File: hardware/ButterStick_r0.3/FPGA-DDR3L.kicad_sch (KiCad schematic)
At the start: 1 part, among them U2 ECP5UM5G_85_CABGA381

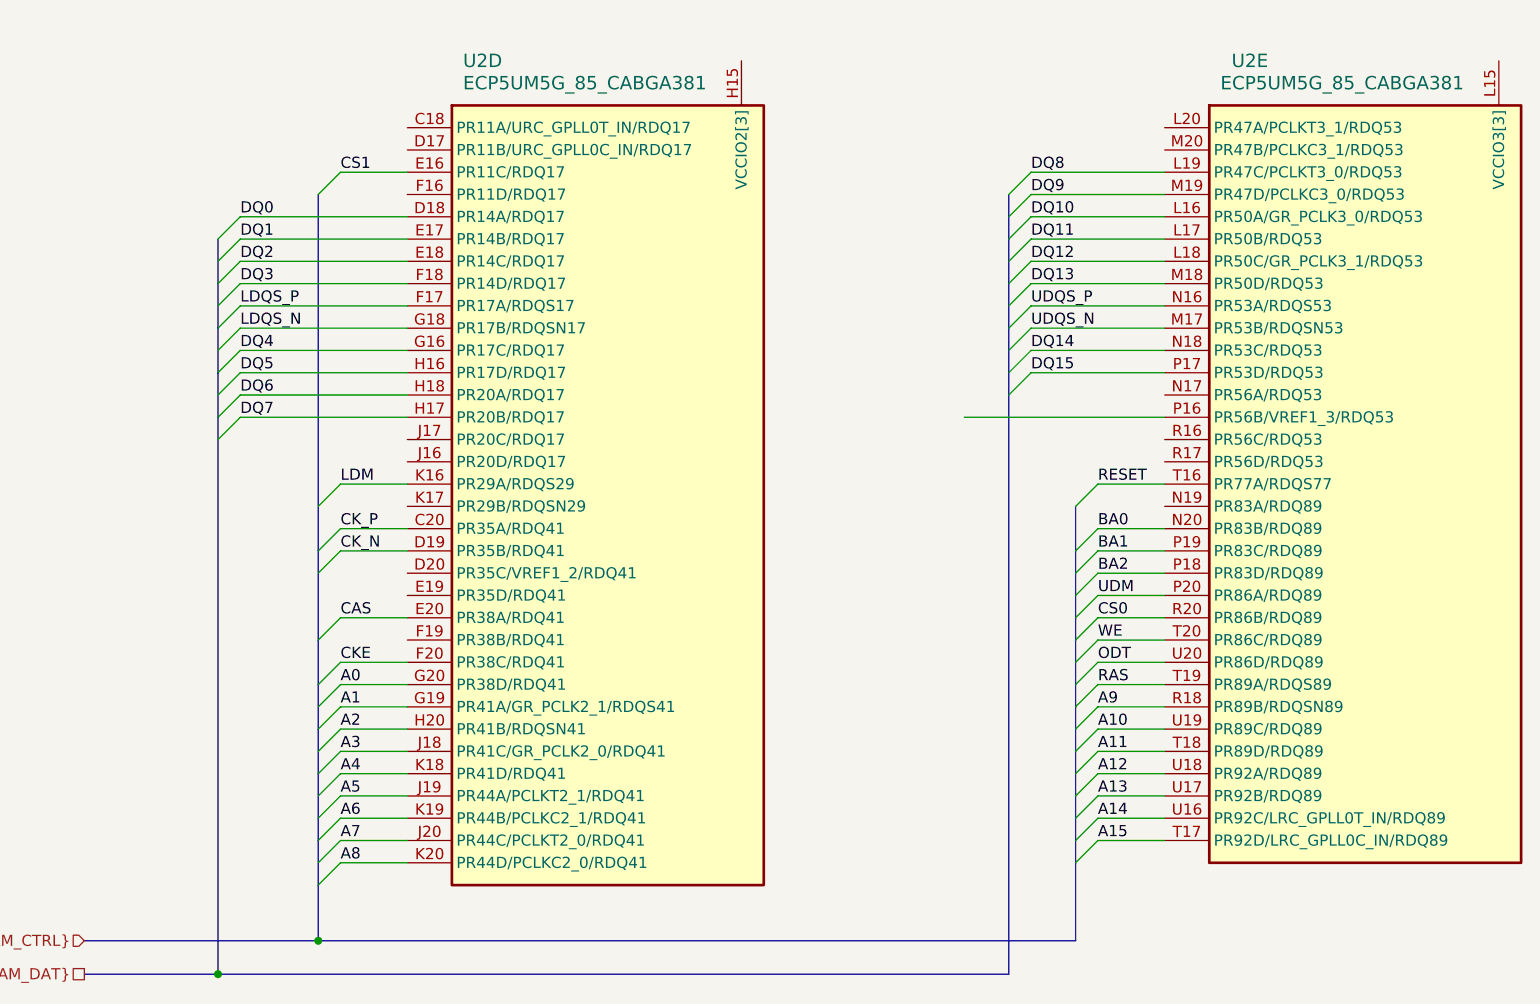
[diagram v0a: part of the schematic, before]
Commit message: hw.r0_3: routing improvements
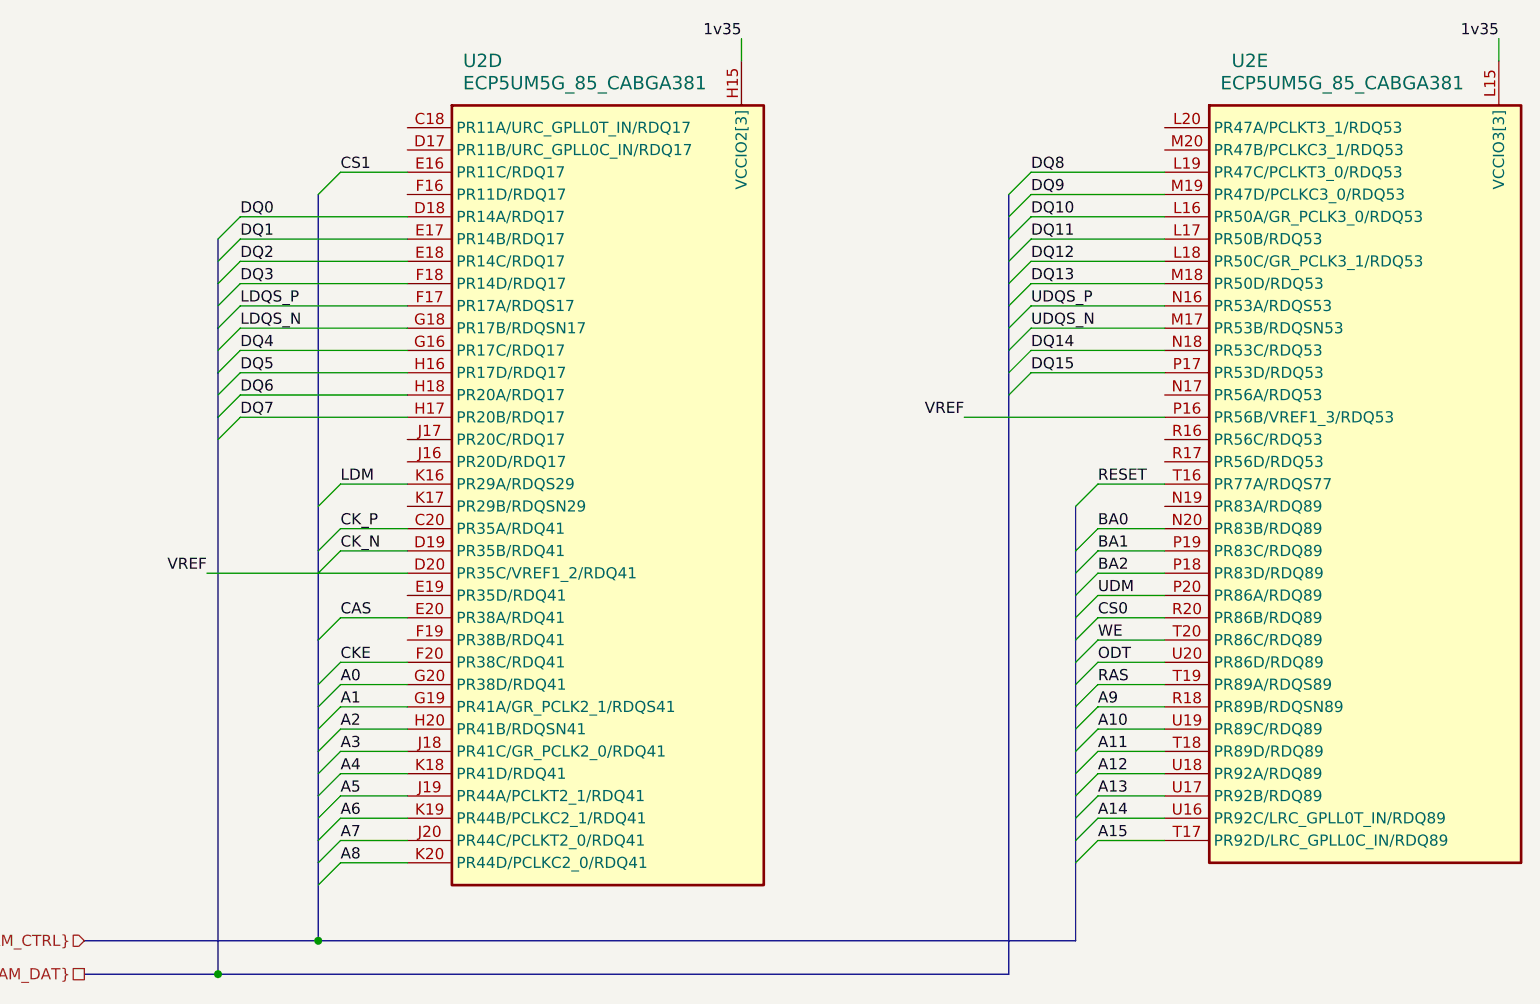
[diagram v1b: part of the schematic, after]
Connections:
- net 1v35: now reaches U2.L14 (VCCIO3[3]), U2.L15 (VCCIO3[3]), U2.M15 (VCCIO3[3])
- net 1v35: now also U2.H14 (VCCIO2[3]), U2.H15 (VCCIO2[3]), U2.J15 (VCCIO2[3])
- net VREF: now reaches U2.P16 (PR56B/VREF1_3/RDQ53)
- net VREF: now also U2.D20 (PR35C/VREF1_2/RDQ41)
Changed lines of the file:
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@@
   (bus_entry (at 168.91 133.35) (size -2.54 2.54))
   (bus_entry (at 168.91 135.89) (size -2.54 2.54))
+  (wire (pts (xy 67.31 105.41) (xy 90.17 105.41)))
   (wire (pts (xy 71.12 64.77) (xy 90.17 64.77)))
   (wire (pts (xy 71.12 67.31) (xy 90.17 67.31)))
@@
   (wire (pts (xy 82.55 135.89) (xy 90.17 135.89)))
   (wire (pts (xy 82.55 138.43) (xy 90.17 138.43)))
+  (wire (pts (xy 128.27 44.45) (xy 128.27 46.99)))
   (wire (pts (xy 153.67 87.63) (xy 176.53 87.63)))
   (wire (pts (xy 161.29 59.69) (xy 176.53 59.69)))
@@
   (wire (pts (xy 168.91 133.35) (xy 176.53 133.35)))
   (wire (pts (xy 168.91 135.89) (xy 176.53 135.89)))
+  (wire (pts (xy 214.63 44.45) (xy 214.63 46.99)))
   (bus (pts (xy 68.58 67.31) (xy 68.58 72.39)))
   (bus (pts (xy 68.58 72.39) (xy 68.58 77.47)))
@@
   (bus (pts (xy 80.01 62.23) (xy 80.01 102.87)))
   (bus (pts (xy 80.01 102.87) (xy 80.01 113.03)))
-  (bus (pts (xy 80.01 113.03) (xy 80.01 118.11)))
-  (bus (pts (xy 80.01 118.11) (xy 80.01 123.19)))
-  (bus (pts (xy 80.01 123.19) (xy 80.01 128.27)))
-  (bus (pts (xy 80.01 128.27) (xy 80.01 133.35)))
-  (bus (pts (xy 80.01 133.35) (xy 80.01 135.89)))
-  (bus (pts (xy 80.01 135.89) (xy 80.01 140.97)))
-  (bus (pts (xy 80.01 140.97) (xy 80.01 147.32)))
+  (bus (pts (xy 80.01 113.03) (xy 80.01 120.65)))
+  (bus (pts (xy 80.01 120.65) (xy 80.01 125.73)))
+  (bus (pts (xy 80.01 125.73) (xy 80.01 130.81)))
+  (bus (pts (xy 80.01 130.81) (xy 80.01 135.89)))
+  (bus (pts (xy 80.01 135.89) (xy 80.01 138.43)))
+  (bus (pts (xy 80.01 138.43) (xy 80.01 147.32)))
   (bus (pts (xy 80.01 147.32) (xy 53.34 147.32)))
   (bus (pts (xy 158.75 62.23) (xy 158.75 67.31)))
   (bus (pts (xy 158.75 67.31) (xy 158.75 72.39)))
-  (bus (pts (xy 158.75 72.39) (xy 158.75 77.47)))
-  (bus (pts (xy 158.75 77.47) (xy 158.75 82.55)))
-  (bus (pts (xy 158.75 82.55) (xy 158.75 151.13)))
+  (bus (pts (xy 158.75 72.39) (xy 158.75 74.93)))
+  (bus (pts (xy 158.75 74.93) (xy 158.75 80.01)))
+  (bus (pts (xy 158.75 80.01) (xy 158.75 85.09)))
+  (bus (pts (xy 158.75 85.09) (xy 158.75 151.13)))
   (bus (pts (xy 158.75 151.13) (xy 68.58 151.13)))
   (bus (pts (xy 166.37 97.79) (xy 166.37 102.87)))
   (bus (pts (xy 166.37 102.87) (xy 166.37 107.95)))
-  (bus (pts (xy 166.37 107.95) (xy 166.37 110.49)))
-  (bus (pts (xy 166.37 110.49) (xy 166.37 115.57)))
-  (bus (pts (xy 166.37 115.57) (xy 166.37 118.11)))
-  (bus (pts (xy 166.37 118.11) (xy 166.37 123.19)))
-  (bus (pts (xy 166.37 123.19) (xy 166.37 125.73)))
+  (bus (pts (xy 166.37 107.95) (xy 166.37 113.03)))
+  (bus (pts (xy 166.37 113.03) (xy 166.37 115.57)))
+  (bus (pts (xy 166.37 115.57) (xy 166.37 120.65)))
+  (bus (pts (xy 166.37 120.65) (xy 166.37 125.73)))
   (bus (pts (xy 166.37 125.73) (xy 166.37 130.81)))
   (bus (pts (xy 166.37 130.81) (xy 166.37 135.89)))
   (bus (pts (xy 166.37 135.89) (xy 166.37 147.32)))
   (bus (pts (xy 166.37 147.32) (xy 80.01 147.32)))
+  (label "VREF" (at 67.31 105.41 180)
+    (effects (font (size 1.27 1.27)) (justify right bottom))
+  )
   (label "DQ0" (at 71.12 64.77 0)
     (effects (font (size 1.27 1.27)) (justify left bottom))
@@
     (effects (font (size 1.27 1.27)) (justify left bottom))
   )
+  (label "1v35" (at 128.27 44.45 180)
+    (effects (font (size 1.27 1.27)) (justify right bottom))
+  )
+  (label "VREF" (at 153.67 87.63 180)
+    (effects (font (size 1.27 1.27)) (justify right bottom))
+  )
   (label "DQ8" (at 161.29 59.69 0)
     (effects (font (size 1.27 1.27)) (justify left bottom))
@@
     (effects (font (size 1.27 1.27)) (justify left bottom))
   )
+  (label "1v35" (at 214.63 44.45 180)
+    (effects (font (size 1.27 1.27)) (justify right bottom))
+  )
   (hierarchical_label "{DRAM_CTRL}" (shape input) (at 53.34 147.32 180)

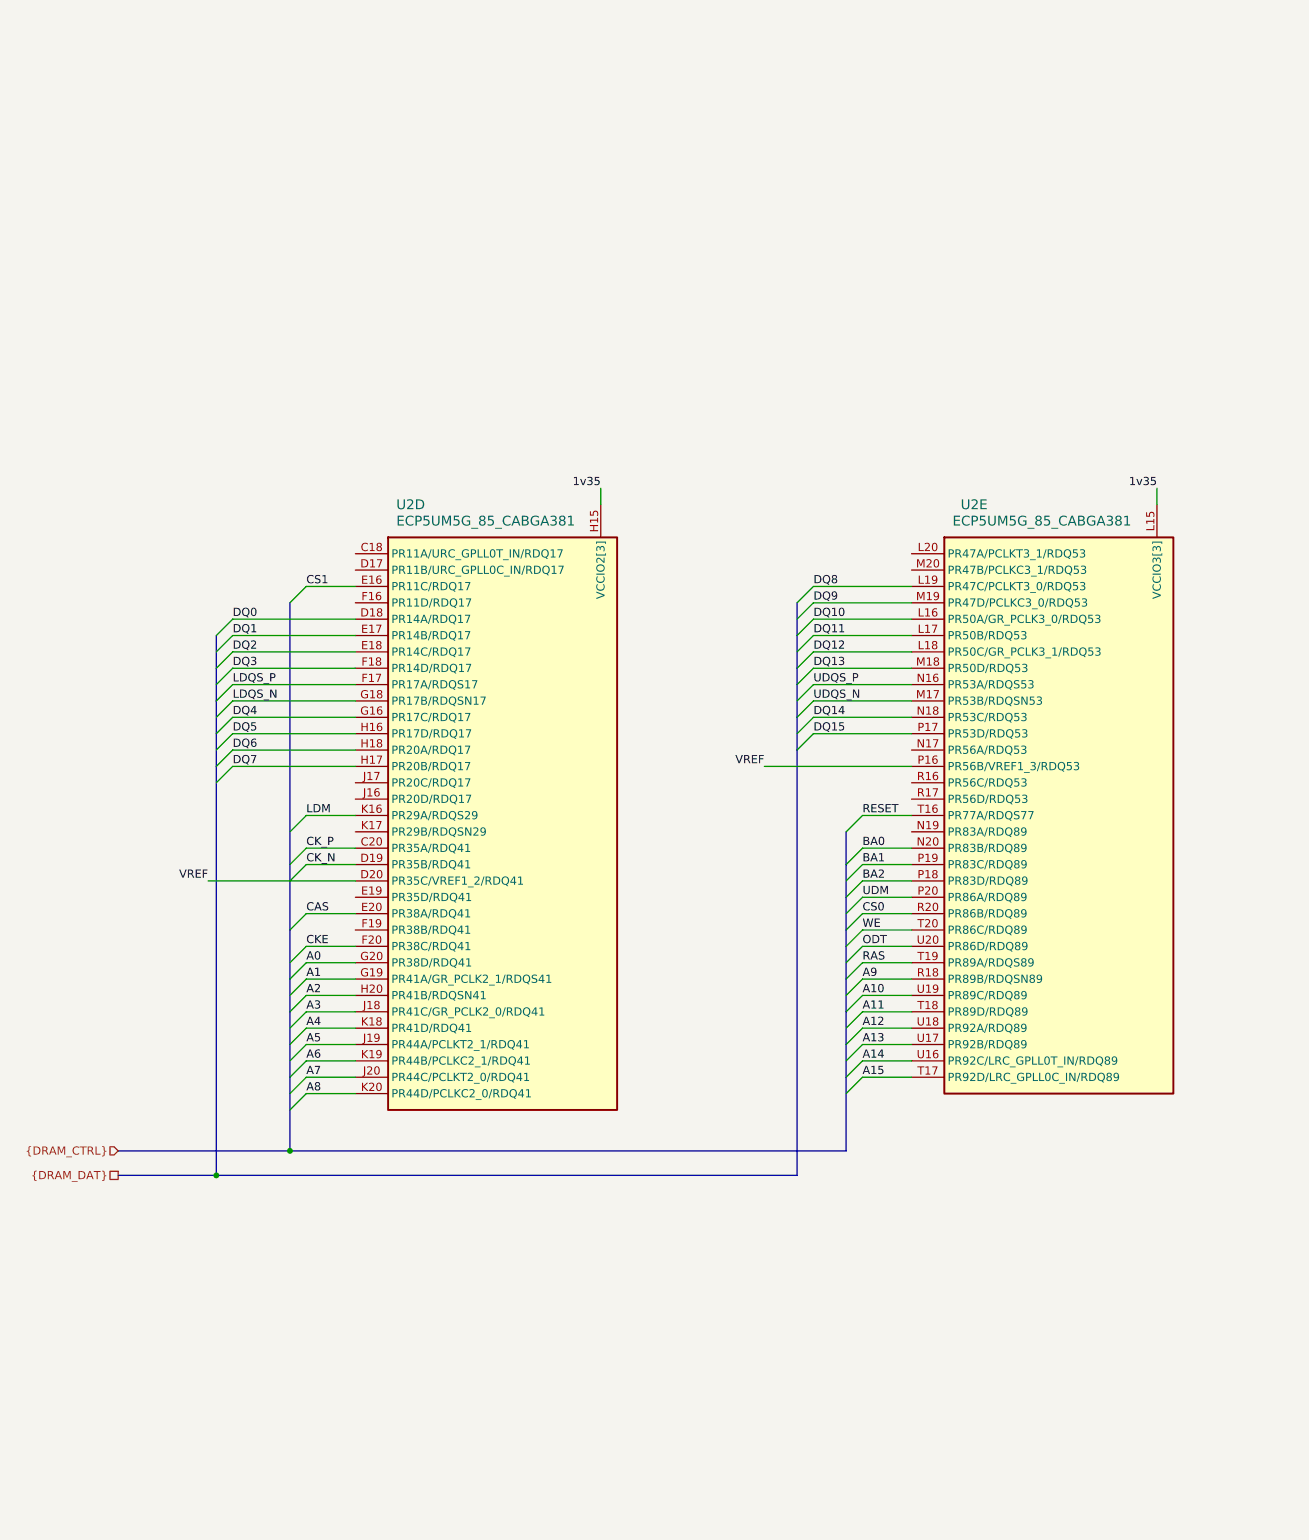
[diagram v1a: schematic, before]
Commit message: hw.r0_3: Start routing DDR3 interface
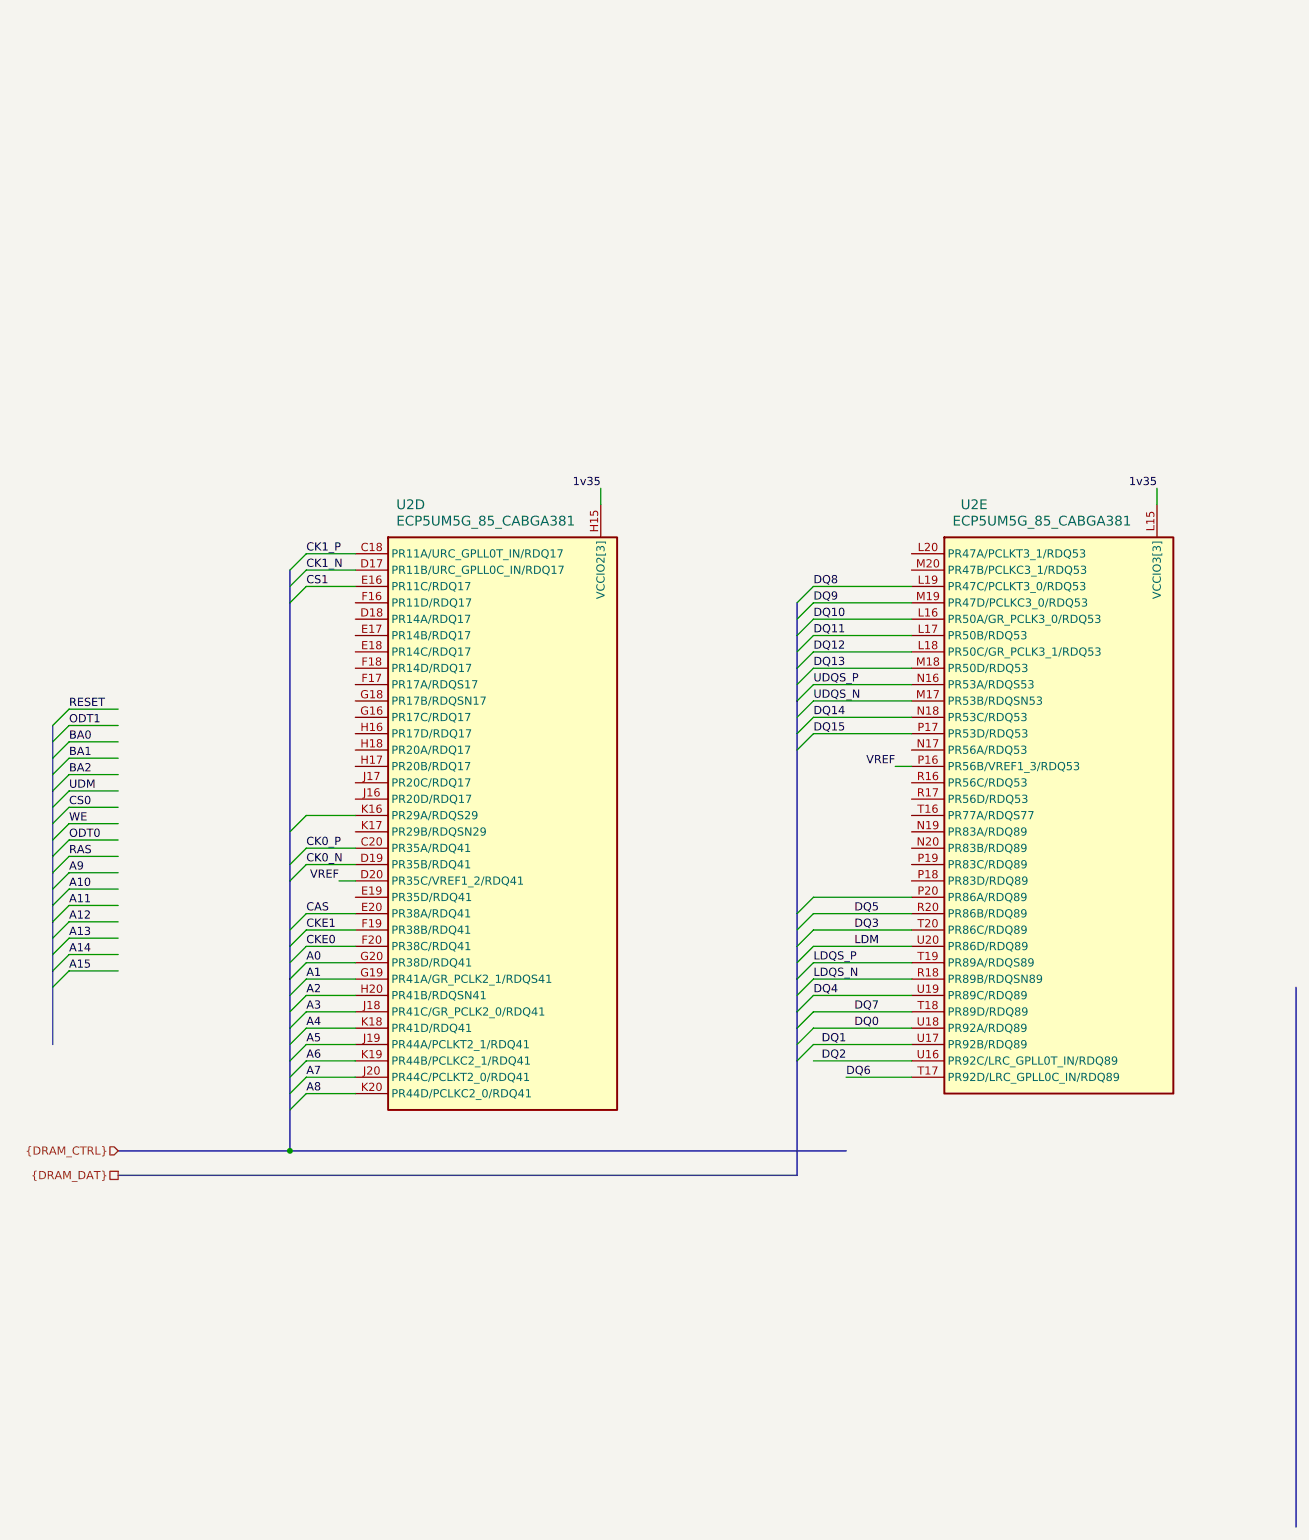
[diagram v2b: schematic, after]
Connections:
- net ODT is gone; now on net LDM: U2.U20 (PR86D/RDQ89)
- net A10: no longer U2.U19 (PR89C/RDQ89)
- net A11: no longer U2.T18 (PR89D/RDQ89)
- net A12: no longer U2.U18 (PR92A/RDQ89)
- net A13: no longer U2.U17 (PR92B/RDQ89)
- net A14: no longer U2.U16 (PR92C/LRC_GPLL0T_IN/RDQ89)
- net A15: no longer U2.T17 (PR92D/LRC_GPLL0C_IN/RDQ89)
- net A9: no longer U2.R18 (PR89B/RDQSN89)
- net BA0: no longer U2.N20 (PR83B/RDQ89)
- net BA1: no longer U2.P19 (PR83C/RDQ89)
- net BA2: no longer U2.P18 (PR83D/RDQ89)
- net CS0: no longer U2.R20 (PR86B/RDQ89)
- net DQ0: now also U2.U18 (PR92A/RDQ89); no longer U2.D18 (PR14A/RDQ17)
- net DQ1: now also U2.U17 (PR92B/RDQ89); no longer U2.E17 (PR14B/RDQ17)
- net DQ2: now also U2.U16 (PR92C/LRC_GPLL0T_IN/RDQ89); no longer U2.E18 (PR14C/RDQ17)
- net DQ3: now also U2.T20 (PR86C/RDQ89); no longer U2.F18 (PR14D/RDQ17)
- net DQ4: now also U2.U19 (PR89C/RDQ89); no longer U2.G16 (PR17C/RDQ17)
- net DQ5: now also U2.R20 (PR86B/RDQ89); no longer U2.H16 (PR17D/RDQ17)
- net DQ6: now also U2.T17 (PR92D/LRC_GPLL0C_IN/RDQ89); no longer U2.H18 (PR20A/RDQ17)
- net DQ7: now also U2.T18 (PR89D/RDQ89); no longer U2.H17 (PR20B/RDQ17)
- net LDM: no longer U2.K16 (PR29A/RDQS29)
- net LDQS_N: now also U2.R18 (PR89B/RDQSN89); no longer U2.G18 (PR17B/RDQSN17)
- net LDQS_P: now also U2.T19 (PR89A/RDQS89); no longer U2.F17 (PR17A/RDQS17)
- net RAS: no longer U2.T19 (PR89A/RDQS89)
- net RESET: no longer U2.T16 (PR77A/RDQS77)
- net UDM: no longer U2.P20 (PR86A/RDQ89)
- net WE: no longer U2.T20 (PR86C/RDQ89)
- net CK1_P: now reaches U2.C18 (PR11A/URC_GPLL0T_IN/RDQ17)
- net CK1_N: now reaches U2.D17 (PR11B/URC_GPLL0C_IN/RDQ17)
- net CKE1: now reaches U2.F19 (PR38B/RDQ41)
- net CKE renamed CKE0
- net CK_N renamed CK0_N
- net CK_P renamed CK0_P
